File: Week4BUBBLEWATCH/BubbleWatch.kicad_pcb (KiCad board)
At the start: 2 copper layers, 28 parts, among them J1 Conn_02x02_Counter_Clockwise, J2 Conn_02x02_Counter_Clockwise, J3 Conn_01x05, SW1 SW_Push, SW2 SW_Push, SW3 SW_Push, SW4 SW_Push, U1 RedRetroBubbleDisplay, U2 RedRetroBubbleDisplay, U4 MCP1640BCH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

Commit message: recommited to update project files for kicad
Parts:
- added U3: STM32F030C8Tx, Package_QFP:LQFP-48_7x7mm_P0.5mm, F.Cu at (186.0, 68.0)
- moved U4 72.1 mm to (93.1, 87.0)
- moved BT2 54.2 mm to (82.0, 79.0), turned to 270 degrees
- moved BT1 25.0 mm to (104.0, 79.0), turned to 90 degrees
- moved C5 16.0 mm to (121.7, 106.0)
- moved C6 16.0 mm to (124.5, 106.0)
- moved C9 15.7 mm to (130.4, 121.0)
- moved C1 15.7 mm to (133.3, 121.0)
- moved C2 15.7 mm to (136.1, 121.0)
- moved C3 15.7 mm to (139.0, 121.0)
- moved C4 15.7 mm to (141.8, 121.0)
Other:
- board outline added: 34 x 27 mm

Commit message: Started layout week 4
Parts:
- added REF**: MountingHole_2.2mm_M2, MountingHole:MountingHole_2.2mm_M2, F.Cu at (89.0, 67.0)
- added REF**: MountingHole_2.2mm_M2, MountingHole:MountingHole_2.2mm_M2, F.Cu at (103.0, 67.0)
- added REF**: MountingHole_2.2mm_M2, MountingHole:MountingHole_2.2mm_M2, F.Cu at (103.0, 91.0)
- added REF**: MountingHole_2.2mm_M2, MountingHole:MountingHole_2.2mm_M2, F.Cu at (89.0, 91.0)
- moved U2 113.4 mm to (59.0, 132.0), turned to 45 degrees
- moved U3 99.9 mm to (104.0, 125.0), turned to 45 degrees
- moved U1 83.0 mm to (89.0, 108.0), turned to 330 degrees
- moved C7 77.3 mm to (96.0, 76.0)
- moved R2 77.2 mm to (96.0, 85.0)
- moved R1 77.2 mm to (96.0, 78.0)
- moved L1 67.7 mm to (98.0, 89.0)
- moved J1 62.1 mm to (96.0, 70.0), turned to 180 degrees
- moved J2 37.7 mm to (134.0, 70.0)
- moved SW4 16.0 mm to (168.4, 96.4)
- moved C5 6.00 mm to (121.7, 112.0)
- moved C6 6.00 mm to (124.5, 112.0)
- moved BT2 5.00 mm to (87.0, 79.0)
- moved U4 2.24 mm to (94.0, 89.0), turned to 90 degrees
- moved BT1 1.00 mm to (105.0, 79.0)
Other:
- board size 34 x 27 mm -> 40 x 76.4 mm

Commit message: more layout work for Week 4
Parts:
- added REF**: MountingHole_2.2mm_M2, MountingHole:MountingHole_2.2mm_M2, F.Cu at (125.0, 91.0)
- added REF**: MountingHole_2.2mm_M2, MountingHole:MountingHole_2.2mm_M2, F.Cu at (139.0, 91.0)
- added REF**: MountingHole_2.2mm_M2, MountingHole:MountingHole_2.2mm_M2, F.Cu at (139.0, 67.0)
- added REF**: MountingHole_2.2mm_M2, MountingHole:MountingHole_2.2mm_M2, F.Cu at (125.0, 67.0)
- J2, RN1, RN2, U3: moved to B.Cu
- moved U2 91.3 mm to (121.0, 65.0), turned to 0 degrees
- moved C9 57.4 mm to (96.0, 75.0)
- moved U3 56.4 mm to (138.0, 80.0), turned to 225 degrees
- moved RN1 47.9 mm to (125.0, 85.0)
- moved C1 46.1 mm to (152.3, 79.0)
- moved C2 46.1 mm to (155.1, 79.0)
- moved C3 46.1 mm to (158.0, 79.0)
- moved C4 46.1 mm to (160.8, 79.0)
- moved RN2 45.8 mm to (125.0, 73.0), turned to 180 degrees
- moved C5 42.5 mm to (138.5, 73.0), turned to 45 degrees
- moved U1 41.2 mm to (121.0, 82.0), turned to 0 degrees
- moved SW3 40.9 mm to (134.0, 65.0)
- moved Y1 35.6 mm to (133.0, 95.0), turned to 90 degrees
- moved R3 34.1 mm to (139.0, 82.0)
- moved J3 34.0 mm to (118.0, 74.0)
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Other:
- board size 40 x 76.4 mm -> 77 x 35.6 mm

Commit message: more routing work
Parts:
- moved C4 19.9 mm to (141.0, 77.0)
- moved C3 16.3 mm to (143.8, 71.0)
- moved C2 10.3 mm to (145.0, 77.0)
- moved C1 10.3 mm to (142.0, 79.0)
- moved SW4 7.92 mm to (146.0, 87.0), turned to 270 degrees
- moved C9 5.50 mm to (96.0, 80.5)
- moved R1 3.16 mm to (96.0, 84.0)
- moved Y1 3.16 mm to (136.0, 94.0), turned to 180 degrees
- moved U1 2.27 mm to (123.0, 80.9)
- moved J3 2.24 mm to (120.0, 73.0)
- moved C5 2.00 mm to (140.5, 73.0)
- moved C6 2.00 mm to (138.0, 80.0)
- moved C8 2.00 mm to (145.0, 73.5)
- moved J2 2.00 mm to (134.0, 69.0)
- moved R3 2.00 mm to (141.0, 82.0)
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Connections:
- J1 pad 4: /+3.3v -> +3V3
- J2 pad 4: /+3.3v -> +3V3
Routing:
- net +BATT: track 0.00 -> 32.5 mm, vias 0 -> 2
- net +3V3: track 0.00 -> 21.0 mm
- net Net-(R1-Pad2): track 0.00 -> 7.15 mm
- net Net-(L1-Pad2): track 0.00 -> 2.96 mm
- net GND: vias 0 -> 2
- added copper zone on F.Cu, net +BATT
- added copper zone on F.Cu, net GND
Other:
- board size 77 x 35.6 mm -> 72 x 33.4 mm
- net class fattrack added: clearance 0.2, trace_width 1, via_dia 0.8, via_drill 0.4

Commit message: More work on week 4
Converting display placements to SMT to allow mor room on board.
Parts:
- BT1, BT2: footprint Battery_Holders:Keystone_3000_1x12mm-CoinCell -> Battery:BatteryHolder_Keystone_3000_1x12mm
- C1, C2, C3, C4, C5, C6, C7, C8, C9: footprint Capacitors_SMD:C_0603 -> Capacitor_SMD:C_0603_1608Metric
- J1, J2: footprint Pin_Headers:Pin_Header_Straight_2x02_Pitch2.54mm_SMD -> Connector_PinHeader_2.54mm:PinHeader_2x02_P2.54mm_Vertical_SMD
- J3: footprint Pin_Headers:Pin_Header_Straight_1x05_Pitch2.54mm -> Connector_Harwin:Harwin_M20-89005xx_1x05_P2.54mm_Horizontal
- L1: footprint Inductors_SMD:L_Taiyo-Yuden_NR-30xx -> Inductor_SMD:L_Taiyo-Yuden_NR-30xx
- R1, R2, R3: footprint Resistors_SMD:R_0603 -> Resistor_SMD:R_0603_1608Metric
- RN1, RN2: footprint Resistors_SMD:R_Array_Concave_4x0402 -> Resistor_SMD:R_Array_Concave_4x0402
- SW1: footprint Buttons_Switches_SMD:SW_SPST_B3U-3000P-B -> Button_Switch_SMD:Panasonic_EVQPUM_EVQPUD
- SW2, SW3: footprint Buttons_Switches_SMD:SW_SPST_B3U-3000P-B -> Button_Switch_SMD:SW_SPST_B3U-3000P; moved to B.Cu
- SW4: footprint Buttons_Switches_SMD:SW_SPST_B3U-3000P-B -> Button_Switch_SMD:SW_SPST_B3U-3000P
- U1, U2: footprint Housings_DIP:DIP-12_W7.62mm_Socket_LongPads -> Package_DIP:DIP-12_W7.62mm_SMDSocket_SmallPads
- U4: footprint TO_SOT_Packages_SMD:SOT-23-6 -> Package_TO_SOT_SMD:SOT-23-6
- Y1: footprint Crystals:Crystal_DS10_d1.0mm_l4.3mm_Horizontal -> Crystal:Crystal_DS10_D1.0mm_L4.3mm_Horizontal_1EP_style1
- moved SW3 15.0 mm to (148.0, 74.0), turned to 90 degrees
- moved U1 13.1 mm to (134.0, 88.0)
- moved U2 12.5 mm to (134.0, 71.0)
- moved J3 6.00 mm to (120.0, 79.0), turned to 180 degrees
- moved C6 5.10 mm to (133.0, 79.0)
- moved U3 5.10 mm to (135.0, 79.0)
- moved SW2 1.00 mm to (147.0, 66.0), turned to 90 degrees
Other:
- outline, holes or cut-outs redrawn

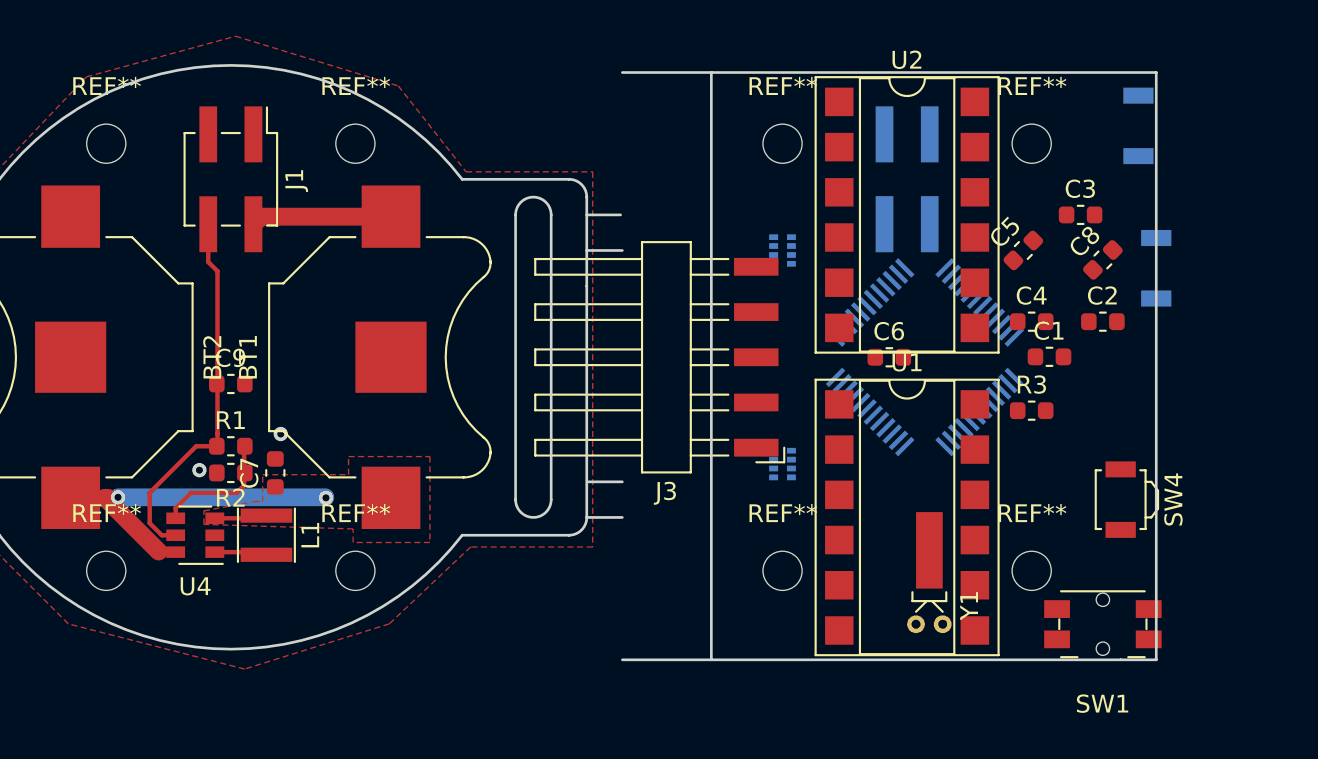
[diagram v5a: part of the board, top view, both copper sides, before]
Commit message: more week 4 board work
full rearangement of pcb an re routing
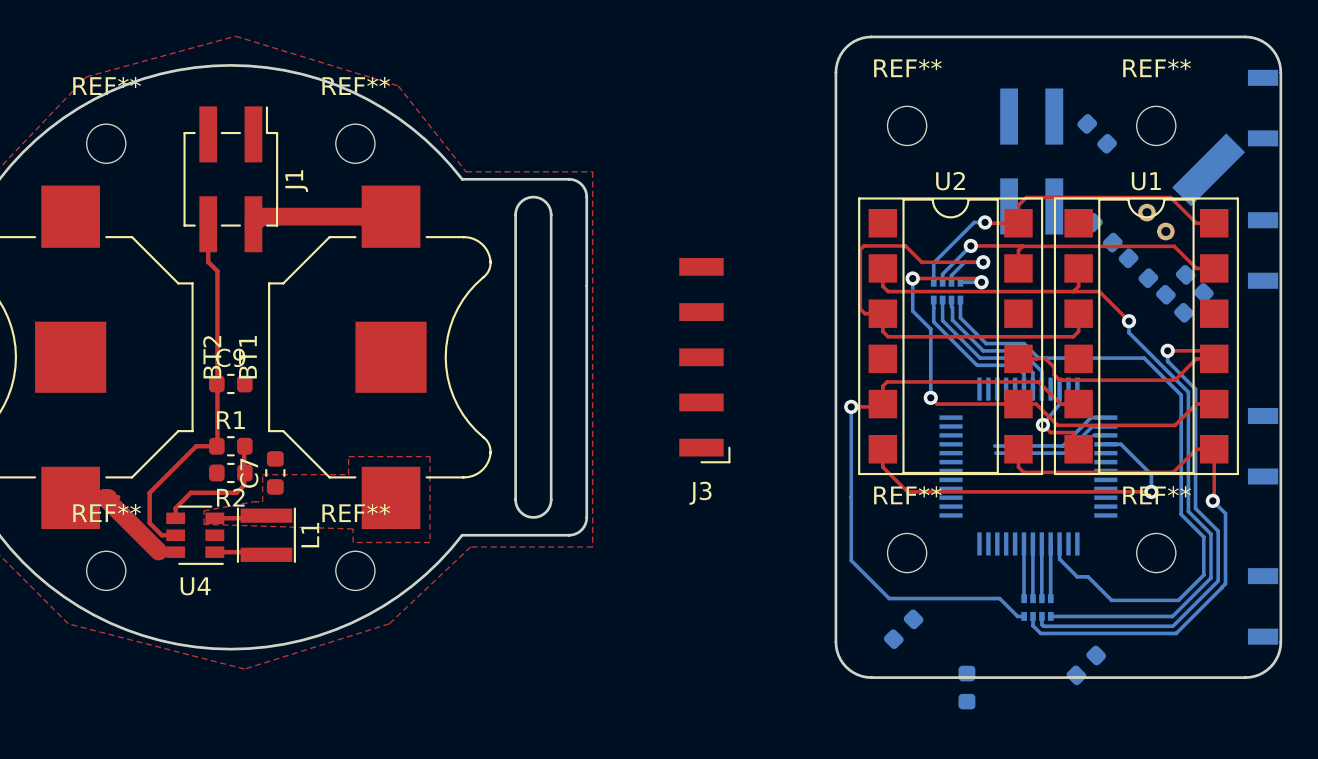
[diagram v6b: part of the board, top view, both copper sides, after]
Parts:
- C1, C2, C3, C4, C5, C6, C8, R3, SW4, Y1: moved to B.Cu
- SW1: footprint Button_Switch_SMD:Panasonic_EVQPUM_EVQPUD -> Buttons_Switches_SMD:SW_SPST_B3U-3000P; moved to B.Cu
- U1: footprint Package_DIP:DIP-12_W7.62mm_SMDSocket_SmallPads -> Week4BUBBLEWATCH:DIP-12_W7.62mm_SMDSocket_SmallPads
- moved SW1 30.4 mm to (154.0, 65.0), turned to 90 degrees
- moved Y1 25.8 mm to (147.5, 70.9), turned to 315 degrees
- moved C3 25.3 mm to (133.8, 94.3), turned to 225 degrees
- moved RN2 24.7 mm to (141.3, 93.1), turned to 270 degrees
- moved C1 17.5 mm to (144.1, 96.3), turned to 225 degrees
- moved U1 16.9 mm to (147.4, 77.8)
- moved R3 16.0 mm to (137.4, 97.6), turned to 90 degrees
- moved C6 13.9 mm to (145.0, 72.0), turned to 135 degrees
- moved RN1 13.4 mm to (136.2, 75.3), turned to 90 degrees
- moved SW3 11.7 mm to (154.0, 84.0)
- moved C2 10.6 mm to (144.7, 66.4), turned to 135 degrees
- moved SW4 10.0 mm to (154.0, 93.0), turned to 90 degrees
- moved SW2 9.90 mm to (154.0, 73.0)
- moved C4 9.17 mm to (150.1, 75.9), turned to 45 degrees
- moved C5 8.78 mm to (149.1, 74.9)
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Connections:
- J3 pad 2: +3V3 -> /RESET
- R3 pad 1: GND -> +3V3
- R3 pad 2: +3V3 -> /RESET
- U3 pad 7: +3V3 -> /RESET
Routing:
- net /SEGE: track 0.00 -> 43.3 mm, vias 0 -> 1
- net /SEGF: track 0.00 -> 40.8 mm, vias 0 -> 1
- net /IOSEGD: track 0.00 -> 36.3 mm
- net /SEGDP: track 0.00 -> 34.1 mm, vias 0 -> 1
- net /SEGG: track 0.00 -> 33.2 mm, vias 0 -> 1
- net /SEGD: track 0.00 -> 29.3 mm, vias 0 -> 3
- net /SEGC: track 0.00 -> 27.8 mm, vias 0 -> 1
- net /DIS8: track 0.00 -> 20.9 mm, vias 0 -> 1
- net /SEGA: track 0.00 -> 19.6 mm, vias 0 -> 1
- net /SEGB: track 0.00 -> 18.4 mm, vias 0 -> 1
- net +BATT: track 32.5 -> 20.3 mm, vias 2 -> 0
- net /IOSEGB: track 0.00 -> 8.36 mm
- net /IOSEGA: track 0.00 -> 8.36 mm
- net /IOSEGC: track 0.00 -> 8.35 mm
- net /DIS5: track 0.00 -> 6.90 mm
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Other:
- board size 72 x 33.4 mm -> 79 x 36 mm
- net class 8mil added: clearance 0.2, trace_width 0.2032, via_dia 0.8, via_drill 0.4

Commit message: more week4 routeing reformated dispaly agiain
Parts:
- moved RN1 46.0 mm to (182.2, 73.8)
- moved U3 36.7 mm to (177.3, 81.1)
- moved RN2 34.2 mm to (175.5, 92.4)
- moved U2 30.5 mm to (164.4, 90.0)
- moved U1 17.3 mm to (164.4, 74.6)
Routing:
- net /IOSEGD: track 36.3 -> 10.6 mm
- net /SEGB: track 18.4 -> 38.9 mm, vias 1 -> 2
- net /SEGA: track 19.6 -> 38.6 mm, vias 1 -> 2
- net /DIS7: track 0.69 -> 16.3 mm
- net /DIS3: track 0.00 -> 14.2 mm
- net /DIS1: track 0.00 -> 12.1 mm
- net /SEGDP: track 34.1 -> 22.4 mm
- net /SEGC: track 27.8 -> 19.1 mm, vias 1 -> 2
- net /IOSEGB: track 8.36 -> 0.00 mm
- net /SEGF: track 40.8 -> 32.8 mm, vias 1 -> 3
- net /IOSEGC: track 8.35 -> 0.44 mm
- net /IOSEGA: track 8.36 -> 0.45 mm
- net /SEGE: track 43.3 -> 35.7 mm, vias 1 -> 2
- net /DIS2: track 0.00 -> 6.62 mm
- net /DIS4: track 5.30 -> 10.1 mm, vias 1 -> 0
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
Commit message: end of day commit
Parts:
- C4, C5, Y1: moved to F.Cu
- moved J3 105.0 mm to (227.0, 78.6), turned to 90 degrees
- moved C8 78.5 mm to (221.1, 99.6)
- moved C4 69.0 mm to (217.6, 90.2), turned to 180 degrees
- moved SW3 67.2 mm to (219.5, 69.2)
- moved Y1 65.4 mm to (210.9, 86.8), turned to 90 degrees
- moved C5 62.2 mm to (209.9, 88.0), turned to 180 degrees
- moved C2 48.2 mm to (173.4, 105.1)
- moved RN1 33.5 mm to (148.9, 70.3)
- moved U1 31.1 mm to (133.6, 70.1)
- moved U2 31.1 mm to (133.6, 85.5)
- moved C1 30.2 mm to (169.7, 112.3)
- moved U3 29.1 mm to (148.4, 77.4)
- moved RN2 27.7 mm to (148.9, 84.5)
- moved SW4 26.3 mm to (175.5, 108.1)
- moved R3 25.3 mm to (156.9, 113.7)
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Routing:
- net /DIS5: track 9.47 -> 39.4 mm, vias 0 -> 1
- net /DIS8: track 20.1 -> 47.1 mm
- net /DIS1: track 12.1 -> 38.3 mm, vias 0 -> 3
- net /SEGC: track 19.1 -> 44.7 mm, vias 2 -> 3
- net /DIS6: track 7.40 -> 31.6 mm, vias 0 -> 1
- net /SEGDP: track 22.4 -> 45.9 mm, vias 1 -> 3
- net /DIS7: track 16.3 -> 39.2 mm, vias 0 -> 1
- net /DIS4: track 10.1 -> 30.0 mm, vias 0 -> 1
- net /DIS2: track 6.62 -> 25.5 mm, vias 0 -> 4
- net /SEGE: track 35.7 -> 54.0 mm, vias 2 -> 4
- net /IOSEGD: track 10.6 -> 28.8 mm, vias 0 -> 4
- net /DIS3: track 14.2 -> 25.7 mm, vias 0 -> 1
- net /SEGD: track 27.3 -> 38.2 mm
- net /SEGG: track 28.5 -> 36.8 mm
- net /SEGB: track 38.9 -> 35.6 mm, vias 2 -> 3
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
